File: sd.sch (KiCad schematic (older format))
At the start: 8 parts, among them J901 Micro_SD_Card_Det, U901 IP4220CZ6, U902 IP4220CZ6

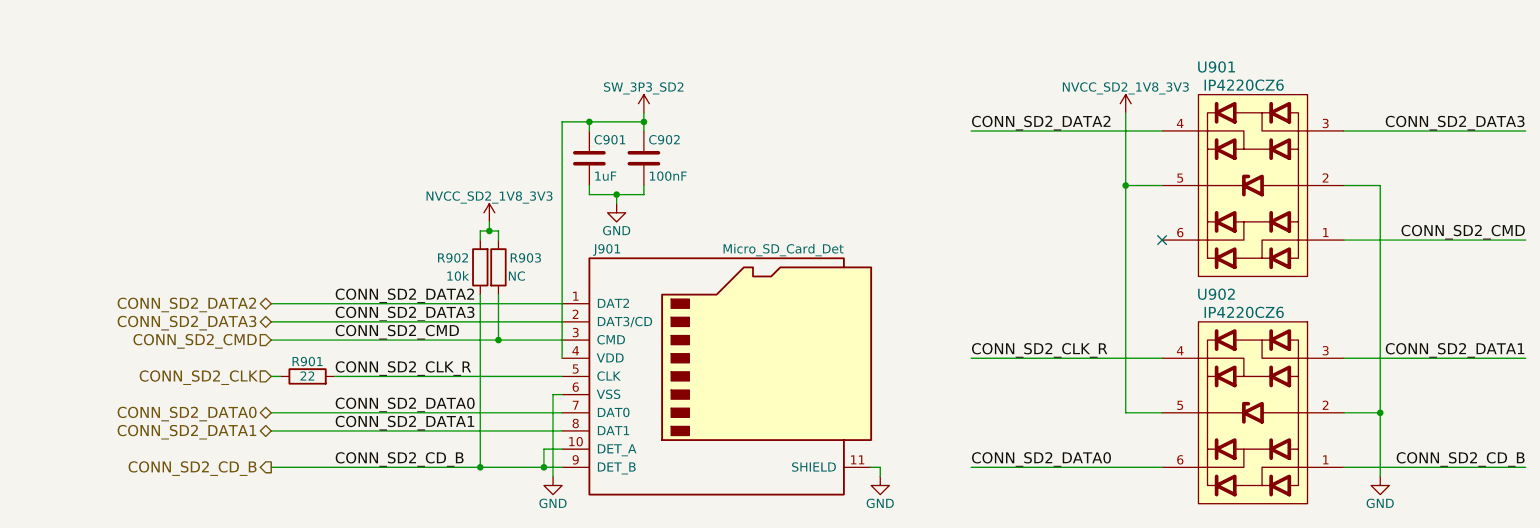
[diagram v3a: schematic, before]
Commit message: Include reverse polarity protection circuit along with a simulation showing its effectiveness
Protecting VBAT from when board is sinking current via USB C. Protects against reverse polarity at the DC jack.

In EmCraft's instance VBUS should only be 5V when sinking current but they must protect against the condition when VBUS>12V and DC_IN=12V. This may need testing.
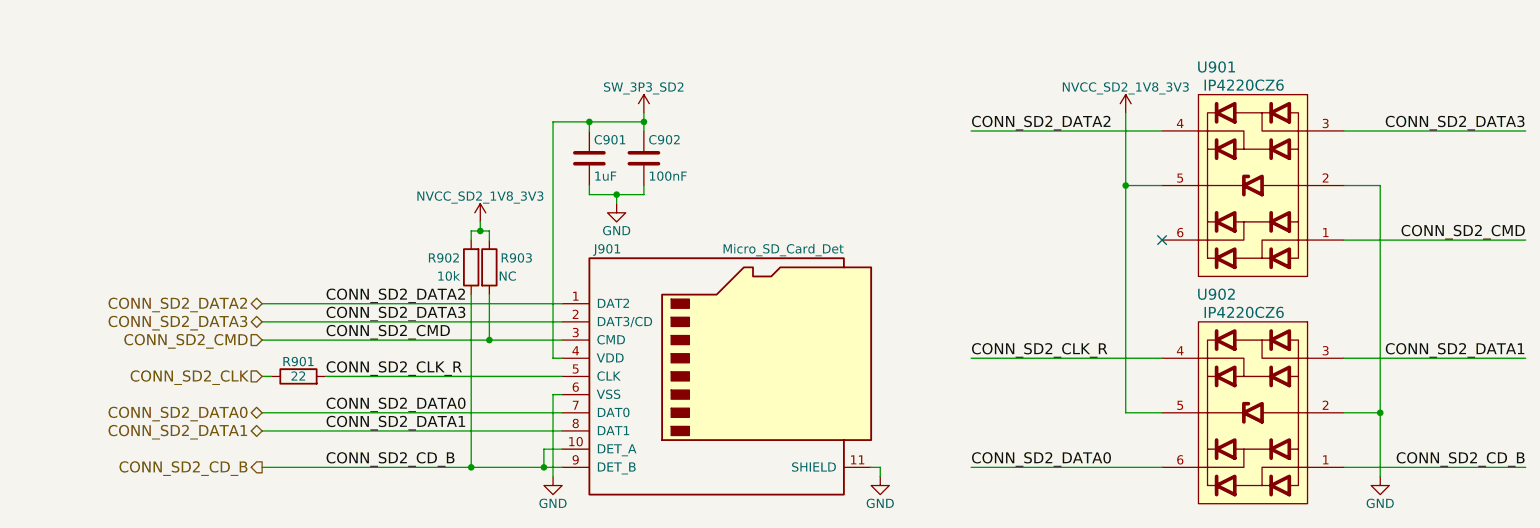
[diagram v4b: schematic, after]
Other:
- moved on the sheet: R901, R902, R903
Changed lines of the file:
@@
 Sheet 9 14
 Title "uSD Card"
-Date "2018-04-16"
+Date "2018-04-18"
 Rev "v0.1.0"
 Comp "Purism SPC"
@@
 	1    0    0    -1
 $EndComp
-Text HLabel 2300 4300 0    60   BiDi ~ 0
+Text HLabel 2250 4300 0    60   BiDi ~ 0
 CONN_SD2_DATA1
-Text HLabel 2300 4200 0    60   BiDi ~ 0
+Text HLabel 2250 4200 0    60   BiDi ~ 0
 CONN_SD2_DATA0
-Text HLabel 2300 3800 0    60   Input ~ 0
+Text HLabel 2250 3800 0    60   Input ~ 0
 CONN_SD2_CMD
-Text HLabel 2300 3700 0    60   BiDi ~ 0
+Text HLabel 2250 3700 0    60   BiDi ~ 0
 CONN_SD2_DATA3
-Text HLabel 2300 3600 0    60   BiDi ~ 0
+Text HLabel 2250 3600 0    60   BiDi ~ 0
 CONN_SD2_DATA2
-Text HLabel 2300 4000 0    60   Input ~ 0
+Text HLabel 2250 4000 0    60   Input ~ 0
 CONN_SD2_CLK
-Text HLabel 2300 4500 0    60   Output ~ 0
+Text HLabel 2250 4500 0    60   Output ~ 0
 CONN_SD2_CD_B
 $Comp
 L R R901
 U 1 1 5AC9FC3A
-P 2500 4000
-F 0 "R901" V 2580 4000 50  0000 C CNN
-F 1 "22" V 2500 4000 50  0000 C CNN
-F 2 "" V 2430 4000 50  0001 C CNN
-F 3 "" H 2500 4000 50  0001 C CNN
-	1    2500 4000
+P 2450 4000
+F 0 "R901" V 2530 4000 50  0000 C CNN
+F 1 "22" V 2450 4000 50  0000 C CNN
+F 2 "" V 2380 4000 50  0001 C CNN
+F 3 "" H 2450 4000 50  0001 C CNN
+	1    2450 4000
 	0    -1   -1   0
 $EndComp
@@
 L R R902
 U 1 1 5ACA0594
-P 3450 3400
-F 0 "R902" H 3600 3350 50  0000 C CNN
-F 1 "10k" H 3575 3450 50  0000 C CNN
-F 2 "" V 3380 3400 50  0001 C CNN
-F 3 "" H 3450 3400 50  0001 C CNN
-	1    3450 3400
+P 3400 3400
+F 0 "R902" H 3550 3350 50  0000 C CNN
+F 1 "10k" H 3525 3450 50  0000 C CNN
+F 2 "" V 3330 3400 50  0001 C CNN
+F 3 "" H 3400 3400 50  0001 C CNN
+	1    3400 3400
 	-1   0    0    1
 $EndComp
@@
 L R R903
 U 1 1 5ACA05C1
-P 3550 3400
-F 0 "R903" H 3700 3450 50  0000 C CNN
-F 1 "NC" H 3650 3350 50  0000 C CNN
-F 2 "" V 3480 3400 50  0001 C CNN
-F 3 "" H 3550 3400 50  0001 C CNN
-	1    3550 3400
+P 3500 3400
+F 0 "R903" H 3650 3450 50  0000 C CNN
+F 1 "NC" H 3600 3350 50  0000 C CNN
+F 2 "" V 3430 3400 50  0001 C CNN
+F 3 "" H 3500 3400 50  0001 C CNN
+	1    3500 3400
 	1    0    0    -1
 $EndComp
@@
 L NVCC_SD2_1V8_3V3 #PWR0124
 U 1 1 5ACA0C17
-P 3500 3150
-F 0 "#PWR0124" H 3500 3000 50  0001 C CNN
-F 1 "NVCC_SD2_1V8_3V3" H 3500 3290 50  0000 C CNN
-F 2 "" H 3500 3150 50  0001 C CNN
-F 3 "" H 3500 3150 50  0001 C CNN
-	1    3500 3150
+P 3450 3150
+F 0 "#PWR0124" H 3450 3000 50  0001 C CNN
+F 1 "NVCC_SD2_1V8_3V3" H 3450 3290 50  0000 C CNN
+F 2 "" H 3450 3150 50  0001 C CNN
+F 3 "" H 3450 3150 50  0001 C CNN
+	1    3450 3150
 	1    0    0    -1
 $EndComp
@@
 $EndComp
 Wire Wire Line
-	2300 3600 3900 3600
-Wire Wire Line
-	2300 3700 3900 3700
-Wire Wire Line
-	2300 3800 3550 3800
-Wire Wire Line
-	3550 3800 3900 3800
-Wire Wire Line
-	2300 4200 3900 4200
-Wire Wire Line
-	2300 4300 3900 4300
-Wire Wire Line
-	2300 4500 3450 4500
-Wire Wire Line
-	3450 4500 3800 4500
-Wire Wire Line
-	3800 4500 3900 4500
+	2250 3600 3900 3600
+Wire Wire Line
+	2250 3700 3900 3700
+Wire Wire Line
+	2250 3800 3900 3800
+Wire Wire Line
+	2250 4200 3900 4200
+Wire Wire Line
+	2250 4300 3900 4300
+Wire Wire Line
+	2250 4500 3900 4500
 Wire Wire Line
 	3900 4400 3800 4400
@@
 	5650 4500 5600 4500
 Wire Wire Line
-	2300 4000 2350 4000
-Wire Wire Line
-	2650 4000 3900 4000
+	2250 4000 2300 4000
+Wire Wire Line
+	2600 4000 3900 4000
 Wire Wire Line
 	3850 4550 3850 4100
@@
 	3850 4100 3900 4100
 Wire Wire Line
-	3450 3250 3450 3200
-Wire Wire Line
-	3550 3200 3550 3250
-Wire Wire Line
-	3450 3200 3500 3200
-Wire Wire Line
-	3500 3200 3550 3200
-Wire Wire Line
-	3500 3150 3500 3200
-Connection ~ 3500 3200
-Wire Wire Line
-	3900 3900 3900 2600
-Wire Wire Line
-	3900 2600 4050 2600
-Wire Wire Line
-	4050 2600 4350 2600
-Wire Wire Line
-	4350 2550 4350 2600
-Wire Wire Line
-	4350 2600 4350 2650
+	3400 3250 3400 3200
+Wire Wire Line
+	3500 3200 3500 3250
+Wire Wire Line
+	3400 3200 3500 3200
+Wire Wire Line
+	3450 3150 3450 3200
+Connection ~ 3450 3200
+Wire Wire Line
+	3850 3900 3850 2600
+Wire Wire Line
+	3850 2600 4350 2600
+Wire Wire Line
+	4350 2550 4350 2650
 Wire Wire Line
 	4050 2650 4050 2600
@@
 	4050 2950 4050 3000
 Wire Wire Line
-	4050 3000 4200 3000
-Wire Wire Line
-	4200 3000 4350 3000
+	4050 3000 4350 3000
 Wire Wire Line
 	4350 3000 4350 2950
@@
 Connection ~ 4350 2600
 Wire Wire Line
-	3450 3550 3450 4500
-Connection ~ 3450 4500
-Wire Wire Line
-	3550 3550 3550 3800
-Connection ~ 3550 3800
+	3400 3550 3400 4500
+Connection ~ 3400 4500
+Wire Wire Line
+	3500 3550 3500 3800
+Connection ~ 3500 3800
 $Comp
 L IP4220CZ6 U901
@@
 $EndComp
 Wire Wire Line
-	8400 2950 8400 4200
-Wire Wire Line
-	8400 4200 8400 4550
+	8400 2950 8400 4550
 Wire Wire Line
 	8400 4200 8200 4200
@@
 $EndComp
 Wire Wire Line
-	7000 2550 7000 2950
-Wire Wire Line
-	7000 2950 7000 4200
+	7000 2550 7000 4200
 Wire Wire Line
 	7000 4200 7200 4200
@@
 Wire Wire Line
 	7200 3900 6150 3900
-Text Label 2650 3600 0    60   ~ 0
+Text Label 2600 3600 0    60   ~ 0
 CONN_SD2_DATA2
-Text Label 2650 4000 0    60   ~ 0
+Text Label 2600 4000 0    60   ~ 0
 CONN_SD2_CLK_R
-Text Label 2650 4200 0    60   ~ 0
+Text Label 2600 4200 0    60   ~ 0
 CONN_SD2_DATA0
-Text Label 2650 3700 0    60   ~ 0
+Text Label 2600 3700 0    60   ~ 0
 CONN_SD2_DATA3
-Text Label 2650 3800 0    60   ~ 0
+Text Label 2600 3800 0    60   ~ 0
 CONN_SD2_CMD
-Text Label 2650 4300 0    60   ~ 0
+Text Label 2600 4300 0    60   ~ 0
 CONN_SD2_DATA1
-Text Label 2650 4500 0    60   ~ 0
+Text Label 2600 4500 0    60   ~ 0
 CONN_SD2_CD_B
+Wire Wire Line
+	3850 3900 3900 3900
 $EndSCHEMATC
